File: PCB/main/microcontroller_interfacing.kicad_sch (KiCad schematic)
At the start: 10 parts, among them IC5 CP2102-GMR, J5 USB_B_Micro, U6 CAT24C256

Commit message: Updated all footprints of components
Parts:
- added D7, D8: GREEN, EEE3088F_Footprints:LEDC1608X50N, symbol Device:LED
- added R11, R13: 1K2, EEE3088F_Footprints:RESC1608X55N, symbol Device:R
- C11: renamed from C7; footprint (none) -> EEE3088F_Footprints:CAPC1608X90N
- C12: renamed from C8; footprint (none) -> EEE3088F_Footprints:CAPC1005X55N
- C13: renamed from C9; footprint (none) -> EEE3088F_Footprints:CAPC1005X55N
- D4: renamed from D6; footprint Diode_SMD:D_MiniMELF -> EEE3088F_Footprints:LL-34_L3.5-W1.5-RD
- D5: renamed from D7; footprint Diode_SMD:D_MiniMELF -> EEE3088F_Footprints:LL-34_L3.5-W1.5-RD
- D6: renamed from D8; footprint Diode_SMD:D_MiniMELF -> EEE3088F_Footprints:LL-34_L3.5-W1.5-RD
- IC5: footprint (none) -> EEE3088F_Footprints:QFN50P500X500X100-29N-D
- J5: footprint (none) -> EEE3088F_Footprints:MICROXNJ
- R12: renamed from R13; footprint Resistor_SMD:R_0805_2012Metric -> EEE3088F_Footprints:RESC2013X65N
- U3: renamed from U6; footprint (none) -> EEE3088F_Footprints:SOIC127P600X175-8N
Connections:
- net BEGIN: now also R11.1
- net FTDI_VDD: now also R12.1; no longer R12.2
- net GND: now also D7.1 (K), D8.1 (K)
- net at IC5.12 (SUSPEND): now also R13.1
- net FTDI_RST: no longer names the net of IC5.9 (~{RST})
- net FTDI_RST: now also R12.2; no longer R12.1
- new net: D8.2 (A), R13.2
- new net: D7.2 (A), R11.2
- no-connect marks 20 -> 19
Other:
- note added: "A high value on BEGIN/VBUS indicates to the FTDI that there is a active connection on the USB port."
- note added: "Planned To-Do: Add LED(s) to show a USB connection Add LED(s) to show data transmission to/from both FTDI and MEM"
- note added: "When SUSPEND is driven high, the CP2102 has entered the USB suspend state. i.e., data tranmission has stopped"
- note removed: "A high value on BEGIN indicates to the FTDI that there is a active connection on the USB port."
- note removed: "FTDI_RST can be used to reset the FTDI device when pulled low for more than 15 us"
- note removed: "Planned To-Do: Add LED(s) to show a USB connection Add Button for resetting the FTDI Add LED(s) to show data transmission to/from both FTDI and MEM"
- moved on the sheet: D4, D5, D6, J5, R12

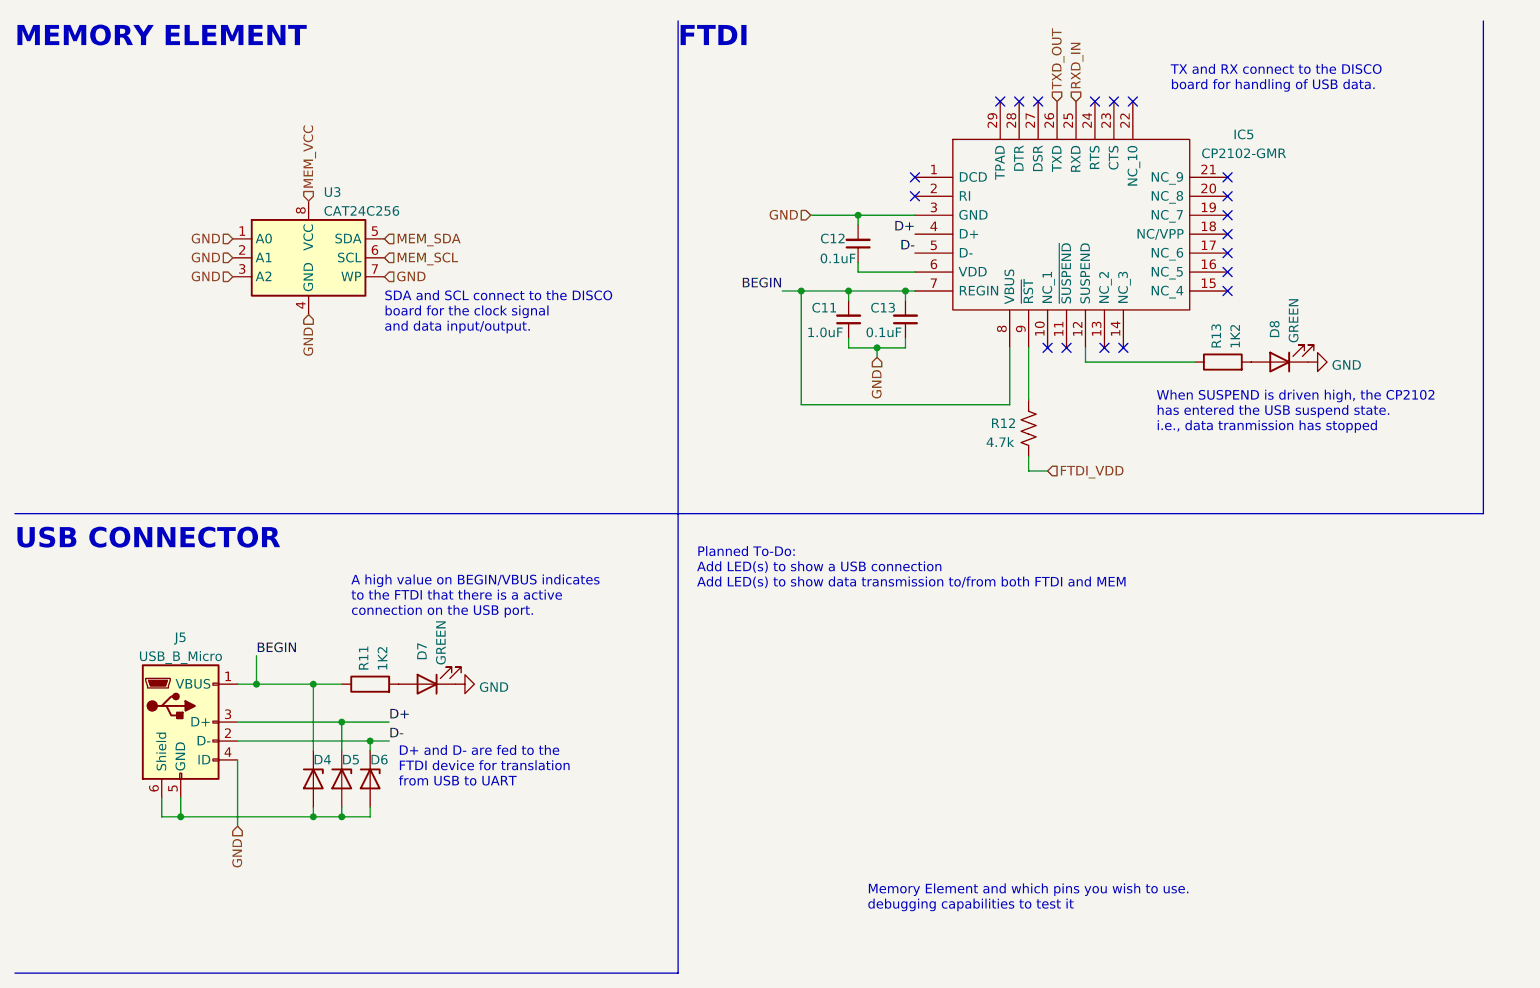
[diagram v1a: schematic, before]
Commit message: Updated labels on schematic
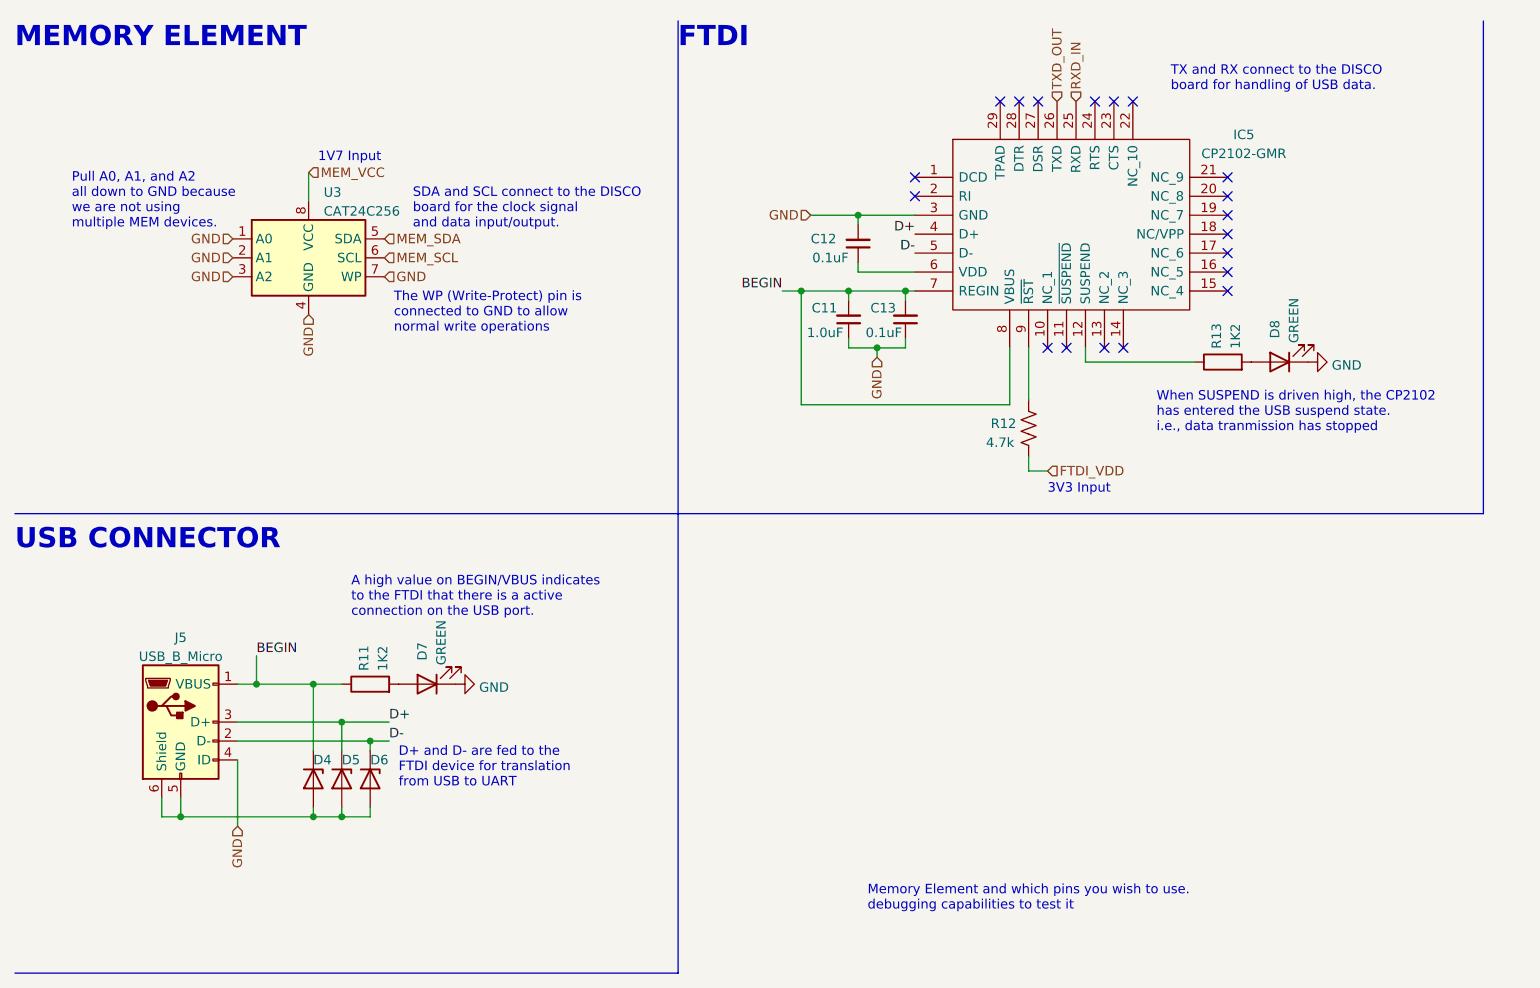
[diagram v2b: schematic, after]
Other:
- note added: "1V7 Input"
- note added: "3V3 Input"
- note added: "Pull A0, A1, and A2 all down to GND because we are not using multiple MEM devices."
- note added: "The WP (Write-Protect) pin is connected to GND to allow normal write operations"
- note removed: "Planned To-Do: Add LED(s) to show a USB connection Add LED(s) to show data transmission to/from both FTDI and MEM"
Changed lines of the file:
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@@
     (title "Microcontroller Interfacing Subsystem")
     (date "2022-03-11")
-    (rev "V0.2")
+    (rev "V0.3")
     (company "University of Cape Town")
     (comment 1 "@Authors David Young (YNGDAV005)")
@@
     (stroke (width 0) (type default) (color 0 0 0 0))
   )
+  (wire (pts (xy 52.07 33.02) (xy 52.07 36.83))
+    (stroke (width 0) (type default) (color 0 0 0 0))
+  )
   (wire (pts (xy 60.325 119.38) (xy 60.325 118.11))
     (stroke (width 0) (type default) (color 0 0 0 0))
@@
     (stroke (width 0) (type default) (color 0 0 0 0))
   )
+  (text "1V7 Input\n" (at 53.34 31.75 0)
+    (effects (font (size 1.27 1.27)) (justify left bottom))
+  )
   (text "SDA and SCL connect to the DISCO\nboard for the clock signal\nand data input/output."
-    (at 62.23 54.61 0)
+    (at 66.04 40.64 0)
     (effects (font (size 1.27 1.27)) (justify left bottom))
   )
@@
     (effects (font (size 2.7 2.7) (thickness 0.254) bold) (justify left bottom))
   )
+  (text "Pull A0, A1, and A2\nall down to GND because\nwe are not using \nmultiple MEM devices."
+    (at 20.32 40.64 0)
+    (effects (font (size 1.27 1.27)) (justify left bottom))
+  )
   (text "MEMORY ELEMENT" (at 12.7 16.51 0)
     (effects (font (size 2.7 2.7) (thickness 0.254) bold) (justify left bottom))
   )
+  (text "The WP (Write-Protect) pin is\nconnected to GND to allow \nnormal write operations"
+    (at 63.5 54.61 0)
+    (effects (font (size 1.27 1.27)) (justify left bottom))
+  )
   (text "TX and RX connect to the DISCO\nboard for handling of USB data."
     (at 167.64 22.225 0)
@@
     (effects (font (size 2.7 2.7) (thickness 0.254) bold) (justify left bottom))
   )
-  (text "Planned To-Do:\nAdd LED(s) to show a USB connection\nAdd LED(s) to show data transmission to/from both FTDI and MEM "
-    (at 104.14 88.9 0)
+  (text "3V3 Input\n" (at 151.13 76.2 0)
     (effects (font (size 1.27 1.27)) (justify left bottom))
   )
@@
     (effects (font (size 1.27 1.27)) (justify right))
   )
-  (hierarchical_label "MEM_VCC" (shape input) (at 52.07 36.83 90)
+  (hierarchical_label "MEM_VCC" (shape input) (at 52.07 33.02 0)
     (effects (font (size 1.27 1.27)) (justify left))
   )
@@
   (symbol (lib_id "Device:C_Small") (at 125.73 42.545 180) (unit 1)
     (in_bom yes) (on_board yes)
-    (property "Reference" "C12" (id 0) (at 120.65 41.91 0)
+    (property "Reference" "C12" (id 0) (at 119.38 41.91 0)
       (effects (font (size 1.27 1.27)) (justify right))
     )
-    (property "Value" "0.1uF" (id 1) (at 125.476 44.577 0)
+    (property "Value" "0.1uF" (id 1) (at 124.46 44.45 0)
       (effects (font (size 1.27 1.27)) (justify left))
     )

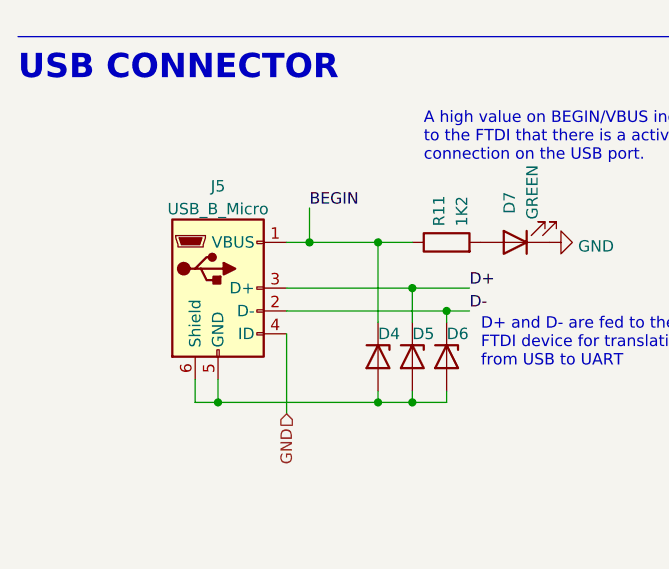
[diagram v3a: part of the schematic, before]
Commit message: Fixed USB footprint and symbol
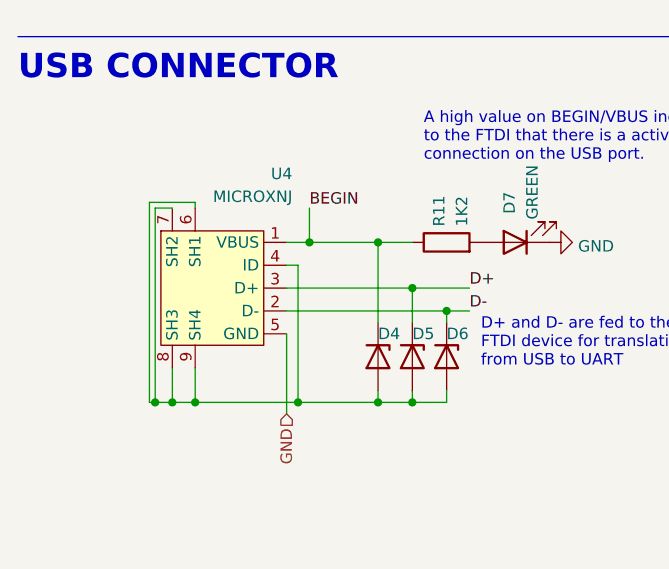
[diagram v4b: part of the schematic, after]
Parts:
- removed J5: USB_B_Micro, EEE3088F_Footprints:MICROXNJ, symbol Connector:USB_B_Micro
- added U4: MICROXNJ, EEE3088F_Footprints:MICRO-USB-SMD_MICROXNJ, symbol AAA_3088F:MICROXNJ
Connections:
- net BEGIN: now also U4.1 (VBUS)
- net D+: now also U4.3 (D+)
- net D-: now also U4.2 (D-)
- net GND: now also U4.5 (GND)
- net at D4.2 (A), D5.2 (A), D6.2 (A): now also U4.4 (ID), U4.6 (SH1), U4.7 (SH2), U4.8 (SH3), U4.9 (SH4)
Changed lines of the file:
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@@
   (junction (at 124.46 48.895) (diameter 0) (color 0 0 0 0)
   )
-  (junction (at 34.925 119.38) (diameter 0) (color 0 0 0 0)
+  (junction (at 43.815 119.38) (diameter 0) (color 0 0 0 0)
+  )
+  (junction (at 27.94 119.38) (diameter 0) (color 0 0 0 0)
   )
   (junction (at 118.11 48.895) (diameter 0) (color 0 0 0 0)
   )
+  (junction (at 29.845 119.38) (diameter 0) (color 0 0 0 0)
+  )
   (junction (at 45.085 101.6) (diameter 0) (color 0 0 0 0)
   )
@@
   )
   (junction (at 52.705 101.6) (diameter 0) (color 0 0 0 0)
+  )
+  (junction (at 32.385 119.38) (diameter 0) (color 0 0 0 0)
   )
   (junction (at 56.515 119.38) (diameter 0) (color 0 0 0 0)
@@
     (stroke (width 0) (type default) (color 0 0 0 0))
   )
-  (wire (pts (xy 32.385 116.84) (xy 32.385 119.38))
+  (wire (pts (xy 29.845 115.57) (xy 29.845 119.38))
     (stroke (width 0) (type default) (color 0 0 0 0))
   )
@@
     (stroke (width 0) (type default) (color 0 0 0 0))
   )
-  (wire (pts (xy 34.925 119.38) (xy 52.705 119.38))
+  (wire (pts (xy 27.305 119.38) (xy 27.94 119.38))
+    (stroke (width 0) (type default) (color 0 0 0 0))
+  )
+  (wire (pts (xy 27.305 97.155) (xy 27.305 119.38))
     (stroke (width 0) (type default) (color 0 0 0 0))
   )
@@
     (stroke (width 0) (type default) (color 0 0 0 0))
   )
+  (wire (pts (xy 27.94 97.79) (xy 27.94 119.38))
+    (stroke (width 0) (type default) (color 0 0 0 0))
+  )
   (wire (pts (xy 115.57 48.895) (xy 118.11 48.895))
     (stroke (width 0) (type default) (color 0 0 0 0))
@@
     (stroke (width 0) (type default) (color 0 0 0 0))
   )
-  (wire (pts (xy 32.385 119.38) (xy 34.925 119.38))
+  (wire (pts (xy 29.845 119.38) (xy 32.385 119.38))
     (stroke (width 0) (type default) (color 0 0 0 0))
   )
@@
     (stroke (width 0) (type default) (color 0 0 0 0))
   )
-  (wire (pts (xy 34.925 116.84) (xy 34.925 119.38))
+  (wire (pts (xy 32.385 115.57) (xy 32.385 119.38))
+    (stroke (width 0) (type default) (color 0 0 0 0))
+  )
+  (wire (pts (xy 43.815 104.14) (xy 43.815 119.38))
     (stroke (width 0) (type default) (color 0 0 0 0))
   )
@@
     (stroke (width 0) (type default) (color 0 0 0 0))
   )
+  (wire (pts (xy 32.385 97.155) (xy 27.305 97.155))
+    (stroke (width 0) (type default) (color 0 0 0 0))
+  )
   (wire (pts (xy 146.05 56.515) (xy 146.05 64.135))
     (stroke (width 0) (type default) (color 0 0 0 0))
@@
     (stroke (width 0) (type default) (color 0 0 0 0))
   )
+  (wire (pts (xy 43.815 119.38) (xy 52.705 119.38))
+    (stroke (width 0) (type default) (color 0 0 0 0))
+  )
+  (wire (pts (xy 32.385 97.79) (xy 32.385 97.155))
+    (stroke (width 0) (type default) (color 0 0 0 0))
+  )
   (wire (pts (xy 124.46 48.895) (xy 124.46 50.165))
     (stroke (width 0) (type default) (color 0 0 0 0))
   )
+  (wire (pts (xy 27.94 119.38) (xy 29.845 119.38))
+    (stroke (width 0) (type default) (color 0 0 0 0))
+  )
+  (wire (pts (xy 29.845 97.79) (xy 27.94 97.79))
+    (stroke (width 0) (type default) (color 0 0 0 0))
+  )
+  (wire (pts (xy 32.385 119.38) (xy 43.815 119.38))
+    (stroke (width 0) (type default) (color 0 0 0 0))
+  )
   (wire (pts (xy 124.46 56.515) (xy 128.27 56.515))
+    (stroke (width 0) (type default) (color 0 0 0 0))
+  )
+  (wire (pts (xy 42.545 104.14) (xy 43.815 104.14))
     (stroke (width 0) (type default) (color 0 0 0 0))
   )
@@
     (pin "2")
   )
-  (symbol (lib_id "Connector:USB_B_Micro") (at 34.925 106.68 0) (unit 1)
+  (symbol (lib_id "Device:C_Small") (at 124.46 52.705 0) (mirror x) (unit 1)
+    (in_bom yes) (on_board yes)
+    (property "Reference" "C11" (id 0) (at 122.936 51.181 0)
+      (effects (font (size 1.27 1.27)) (justify right))
+    )
+    (property "Value" "1.0uF" (id 1) (at 118.872 54.483 0)
+      (effects (font (size 1.27 1.27)) (justify left))
+    )
+    (property "Footprint" "EEE3088F_Footprints:CAPC1608X90N" (id 2) (at 124.46 52.705 0)
+      (effects (font (size 1.27 1.27)) hide)
+    )
+    (property "Datasheet" "~" (id 3) (at 124.46 52.705 0)
+      (effects (font (size 1.27 1.27)) hide)
+    )
+    (pin "1")
+    (pin "2")
+  )
+  (symbol (lib_id "Diode:ZMMxx") (at 52.705 114.3 270) (unit 1)
+    (in_bom yes) (on_board yes)
+    (property "Reference" "D4" (id 0) (at 52.705 111.76 90)
+      (effects (font (size 1.27 1.27)) (justify left))
+    )
+    (property "Value" "ZMMxx" (id 1) (at 54.737 116.0022 90)
+      (effects (font (size 1.27 1.27)) (justify left) hide)
+    )
+    (property "Footprint" "EEE3088F_Footprints:LL-34_L3.5-W1.5-RD" (id 2) (at 48.26 114.3 0)
+      (effects (font (size 1.27 1.27)) hide)
+    )
+    (property "Datasheet" "https://diotec.com/tl_files/diotec/files/pdf/datasheets/zmm1.pdf" (id 3) (at 52.705 114.3 0)
+      (effects (font (size 1.27 1.27)) hide)
+    )
+    (pin "1")
+    (pin "2")
+  )
+  (symbol (lib_id "power:GND") (at 186.055 58.42 90) (unit 1)
     (in_bom yes) (on_board yes) (fields_autoplaced)
-    (property "Reference" "J5" (id 0) (at 34.925 95.3602 0))
-    (property "Value" "USB_B_Micro" (id 1) (at 34.925 97.8971 0))
-    (property "Footprint" "EEE3088F_Footprints:MICROXNJ" (id 2) (at 38.735 107.95 0)
-      (effects (font (size 1.27 1.27)) hide)
-    )
-    (property "Datasheet" "~" (id 3) (at 38.735 107.95 0)
+    (property "Reference" "#PWR019" (id 0) (at 192.405 58.42 0)
+      (effects (font (size 1.27 1.27)) hide)
+    )
+    (property "Value" "GND" (id 1) (at 189.23 58.8538 90)
+      (effects (font (size 1.27 1.27)) (justify right))
+    )
+    (property "Footprint" "" (id 2) (at 186.055 58.42 0)
+      (effects (font (size 1.27 1.27)) hide)
+    )
+    (property "Datasheet" "" (id 3) (at 186.055 58.42 0)
+      (effects (font (size 1.27 1.27)) hide)
+    )
+    (pin "1")
+  )
+  (symbol (lib_id "AAA_3088F:MICROXNJ") (at 33.655 106.68 0) (unit 1)
+    (in_bom yes) (on_board yes)
+    (property "Reference" "U4" (id 0) (at 43.18 93.9831 0)
+      (effects (font (size 1.27 1.27)) (justify right))
+    )
+    (property "Value" "MICROXNJ" (id 1) (at 43.18 96.52 0)
+      (effects (font (size 1.27 1.27)) (justify right))
+    )
+    (property "Footprint" "EEE3088F_Footprints:MICRO-USB-SMD_MICROXNJ" (id 2) (at 33.655 106.68 0)
+      (effects (font (size 1.27 1.27)) hide)
+    )
+    (property "Datasheet" "" (id 3) (at 33.655 106.68 0)
       (effects (font (size 1.27 1.27)) hide)
     )
@@
     (pin "5")
     (pin "6")
-  )
-  (symbol (lib_id "Device:C_Small") (at 124.46 52.705 0) (mirror x) (unit 1)
-    (in_bom yes) (on_board yes)
-    (property "Reference" "C11" (id 0) (at 122.936 51.181 0)
-      (effects (font (size 1.27 1.27)) (justify right))
-    )
-    (property "Value" "1.0uF" (id 1) (at 118.872 54.483 0)
-      (effects (font (size 1.27 1.27)) (justify left))
-    )
-    (property "Footprint" "EEE3088F_Footprints:CAPC1608X90N" (id 2) (at 124.46 52.705 0)
-      (effects (font (size 1.27 1.27)) hide)
-    )
-    (property "Datasheet" "~" (id 3) (at 124.46 52.705 0)
-      (effects (font (size 1.27 1.27)) hide)
-    )
-    (pin "1")
-    (pin "2")
-  )
-  (symbol (lib_id "Diode:ZMMxx") (at 52.705 114.3 270) (unit 1)
-    (in_bom yes) (on_board yes)
-    (property "Reference" "D4" (id 0) (at 52.705 111.76 90)
-      (effects (font (size 1.27 1.27)) (justify left))
-    )
-    (property "Value" "ZMMxx" (id 1) (at 54.737 116.0022 90)
-      (effects (font (size 1.27 1.27)) (justify left) hide)
-    )
-    (property "Footprint" "EEE3088F_Footprints:LL-34_L3.5-W1.5-RD" (id 2) (at 48.26 114.3 0)
-      (effects (font (size 1.27 1.27)) hide)
-    )
-    (property "Datasheet" "https://diotec.com/tl_files/diotec/files/pdf/datasheets/zmm1.pdf" (id 3) (at 52.705 114.3 0)
-      (effects (font (size 1.27 1.27)) hide)
-    )
-    (pin "1")
-    (pin "2")
-  )
-  (symbol (lib_id "power:GND") (at 186.055 58.42 90) (unit 1)
-    (in_bom yes) (on_board yes) (fields_autoplaced)
-    (property "Reference" "#PWR019" (id 0) (at 192.405 58.42 0)
-      (effects (font (size 1.27 1.27)) hide)
-    )
-    (property "Value" "GND" (id 1) (at 189.23 58.8538 90)
-      (effects (font (size 1.27 1.27)) (justify right))
-    )
-    (property "Footprint" "" (id 2) (at 186.055 58.42 0)
-      (effects (font (size 1.27 1.27)) hide)
-    )
-    (property "Datasheet" "" (id 3) (at 186.055 58.42 0)
-      (effects (font (size 1.27 1.27)) hide)
-    )
-    (pin "1")
+    (pin "7")
+    (pin "8")
+    (pin "9")
   )
   (symbol (lib_id "Diode:ZMMxx") (at 60.325 114.3 270) (unit 1)
